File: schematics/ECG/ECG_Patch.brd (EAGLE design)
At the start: 27.3 x 27.3 mm, 6 parts

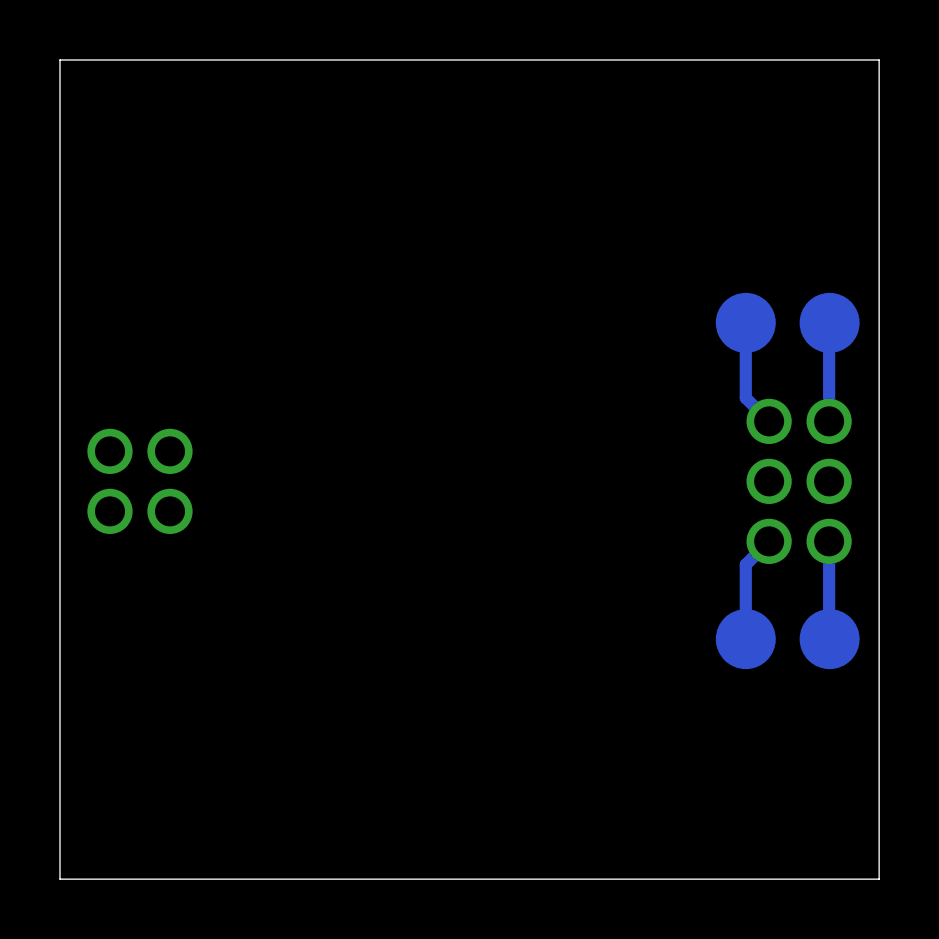
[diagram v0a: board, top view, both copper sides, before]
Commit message: added 4 pin smt header
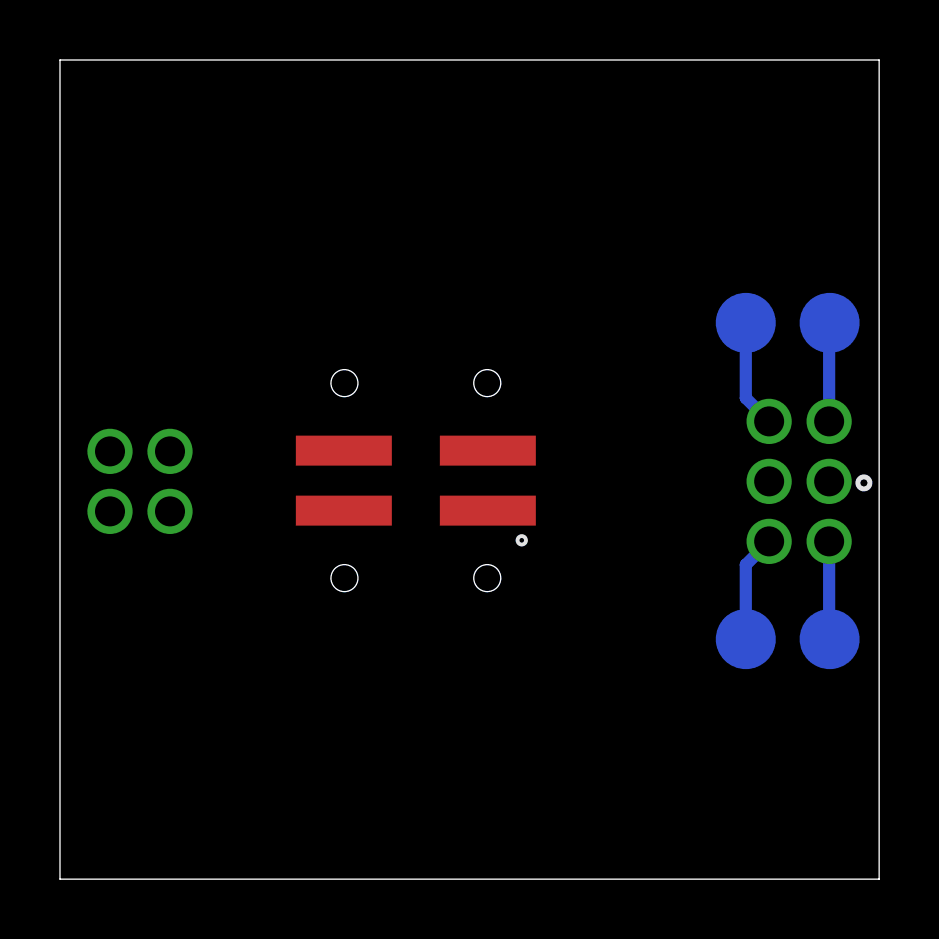
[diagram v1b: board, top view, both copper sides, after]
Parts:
- added U$1: M80-4SMT, harwin:M80-4_SMT
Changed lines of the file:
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@@
 <layer number="43" name="vRestrict" color="2" fill="10" visible="yes" active="yes"/>
 <layer number="44" name="Drills" color="7" fill="1" visible="no" active="yes"/>
-<layer number="45" name="Holes" color="7" fill="1" visible="no" active="yes"/>
+<layer number="45" name="Holes" color="7" fill="1" visible="yes" active="yes"/>
 <layer number="46" name="Milling" color="3" fill="1" visible="no" active="yes"/>
 <layer number="47" name="Measures" color="7" fill="1" visible="no" active="yes"/>
@@
 <wire x1="27.305" y1="27.305" x2="0" y2="27.305" width="0" layer="20"/>
 <wire x1="0" y1="27.305" x2="0" y2="0" width="0" layer="20"/>
+<circle x="26.797" y="13.208" radius="0.08031875" width="0.4064" layer="21"/>
 </plain>
 <attributes>
@@
 <attribute name="TP_SIGNAL_NAME" value="" x="18.5674" y="18.542" size="1.778" layer="28" rot="MR270" display="off"/>
 </element>
+<element name="U$1" library="harwin" package="M80-4_SMT" value="M80-4SMT" x="11.8618" y="13.2842" rot="R90"/>
 </elements>
 <signals>
